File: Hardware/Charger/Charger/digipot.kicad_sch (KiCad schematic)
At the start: 8 parts, among them J1 Conn_01x03, J2 Conn_01x03, J3 Conn_01x03, J4 Conn_01x03, U1 MCP41U83x-xxxx-ST, U2 MCP41U83x-xxxx-ST, U3 MCP41U83x-xxxx-ST, U306 MCP41U83x-xxxx-ST

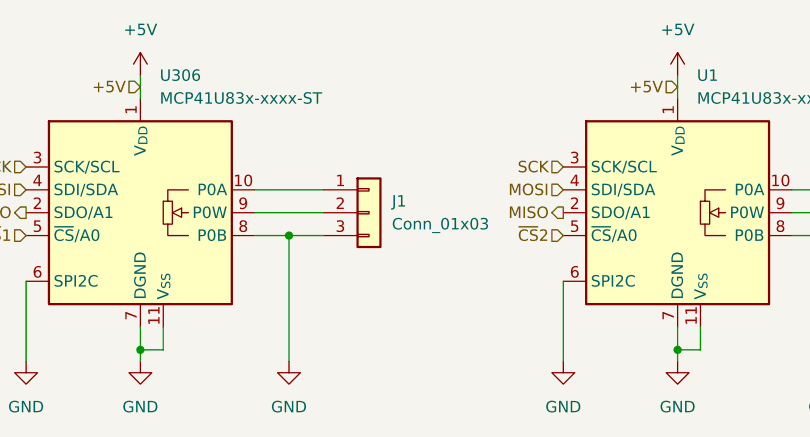
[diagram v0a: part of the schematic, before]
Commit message: Few updates to connectors
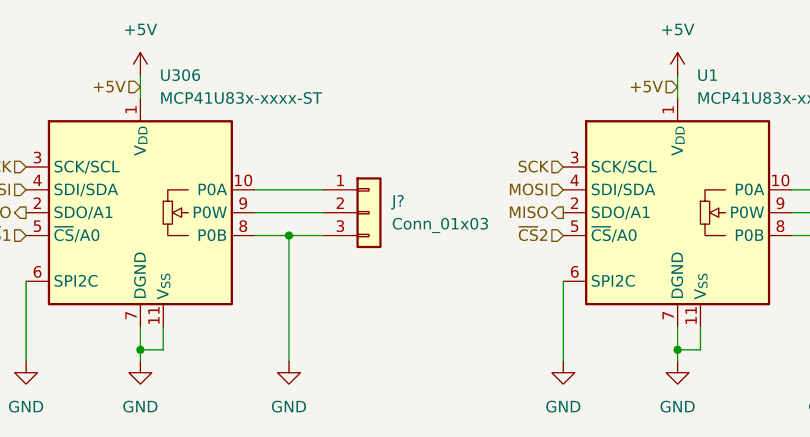
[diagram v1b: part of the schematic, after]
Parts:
- renumbered J1 to J?
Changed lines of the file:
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@@
 		(dnp no)
 		(fields_autoplaced yes)
-		(property "Reference" "#PWR01"
+		(property "Reference" "#PWR?"
 			(at 36.83 72.39 0)
 			(effects
@@
 		(pin "1"
 		)
+		(instances
+			(project "Charger"
+				(path "/ec0cb266-3da5-4155-a0e5-38a3c68d3210/b765b54b-82fb-4d18-b796-af942e7a589a"
+					(reference "#PWR?")
+					(unit 1)
+				)
+			)
+		)
 	)
 	(symbol
@@
 		(dnp no)
 		(fields_autoplaced yes)
-		(property "Reference" "J1"
+		(property "Reference" "J?"
 			(at 77.47 48.2599 0)
 			(effects
@@
 		(pin "3"
 		)
+		(instances
+			(project "Charger"
+				(path "/ec0cb266-3da5-4155-a0e5-38a3c68d3210/b765b54b-82fb-4d18-b796-af942e7a589a"
+					(reference "J?")
+					(unit 1)
+				)
+			)
+		)
 	)
 	(symbol
@@
 		(dnp no)
 		(fields_autoplaced yes)
-		(property "Reference" "#PWR04"
+		(property "Reference" "#PWR?"
 			(at 66.04 72.39 0)
 			(effects
@@
 		(pin "1"
 		)
+		(instances
+			(project "Charger"
+				(path "/ec0cb266-3da5-4155-a0e5-38a3c68d3210/b765b54b-82fb-4d18-b796-af942e7a589a"
+					(reference "#PWR?")
+					(unit 1)
+				)
+			)
+		)
 	)
 	(symbol
@@
 		(dnp no)
 		(fields_autoplaced yes)
-		(property "Reference" "#PWR03"
+		(property "Reference" "#PWR?"
 			(at 49.53 38.1 0)
 			(effects
@@
 		(pin "1"
 		)
-	)
+		(instances
+			(project "Charger"
+				(path "/ec0cb266-3da5-4155-a0e5-38a3c68d3210/b765b54b-82fb-4d18-b796-af942e7a589a"
+					(reference "#PWR?")
+					(unit 1)
+				)
+			)
+		)
+	)

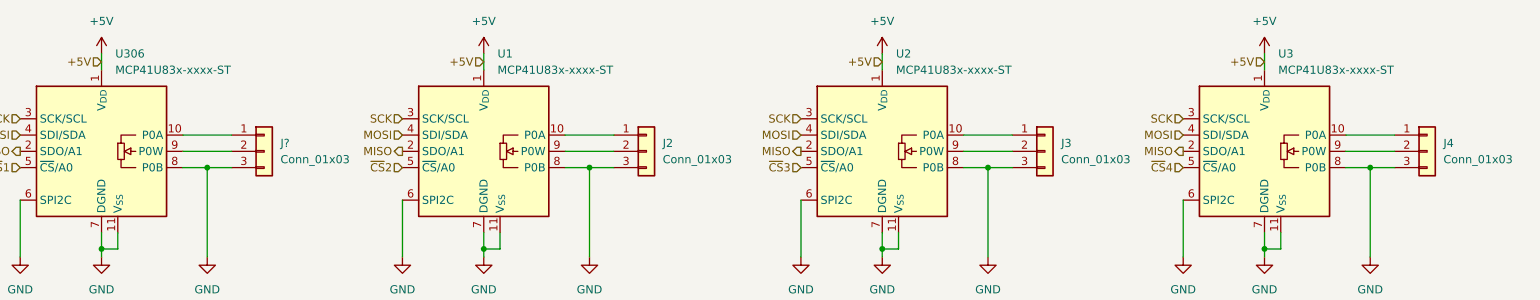
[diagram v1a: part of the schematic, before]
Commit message: Completed PCB layout of charger
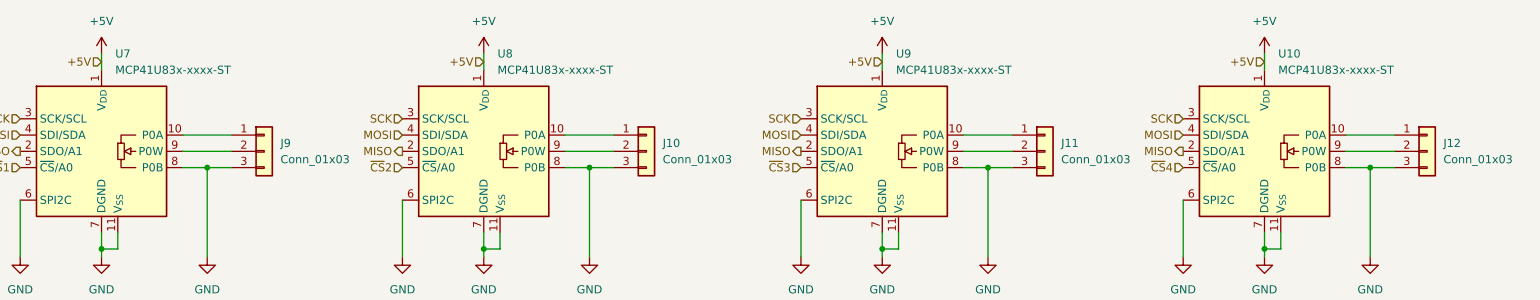
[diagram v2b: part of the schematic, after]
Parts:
- gave numbers to parts that had none: 1
- renumbered J2 to J10, J3 to J11, J4 to J12, U3 to U10, U306 to U7, U1 to U8, U2 to U9
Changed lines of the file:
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@@
 		(dnp no)
 		(fields_autoplaced yes)
-		(property "Reference" "J4"
+		(property "Reference" "J12"
 			(at 259.08 48.2599 0)
 			(effects
@@
 			(project "Charger"
 				(path "/ec0cb266-3da5-4155-a0e5-38a3c68d3210/b765b54b-82fb-4d18-b796-af942e7a589a"
-					(reference "J4")
+					(reference "J12")
 					(unit 1)
 				)
@@
 		(dnp no)
 		(fields_autoplaced yes)
-		(property "Reference" "#PWR?"
+		(property "Reference" "#PWR080"
 			(at 36.83 72.39 0)
 			(effects
@@
 			(project "Charger"
 				(path "/ec0cb266-3da5-4155-a0e5-38a3c68d3210/b765b54b-82fb-4d18-b796-af942e7a589a"
-					(reference "#PWR?")
+					(reference "#PWR080")
 					(unit 1)
 				)
@@
 		(dnp no)
 		(fields_autoplaced yes)
-		(property "Reference" "#PWR08"
+		(property "Reference" "#PWR086"
 			(at 109.22 72.39 0)
 			(effects
@@
 			(project "Charger"
 				(path "/ec0cb266-3da5-4155-a0e5-38a3c68d3210/b765b54b-82fb-4d18-b796-af942e7a589a"
-					(reference "#PWR08")
+					(reference "#PWR086")
 					(unit 1)
 				)
@@
 		(dnp no)
 		(fields_autoplaced yes)
-		(property "Reference" "#PWR09"
+		(property "Reference" "#PWR087"
 			(at 125.73 72.39 0)
 			(effects
@@
 			(project "Charger"
 				(path "/ec0cb266-3da5-4155-a0e5-38a3c68d3210/b765b54b-82fb-4d18-b796-af942e7a589a"
-					(reference "#PWR09")
+					(reference "#PWR087")
 					(unit 1)
 				)
@@
 		(dnp no)
 		(fields_autoplaced yes)
-		(property "Reference" "#PWR07"
+		(property "Reference" "#PWR085"
 			(at 109.22 38.1 0)
 			(effects
@@
 			(project "Charger"
 				(path "/ec0cb266-3da5-4155-a0e5-38a3c68d3210/b765b54b-82fb-4d18-b796-af942e7a589a"
-					(reference "#PWR07")
+					(reference "#PWR085")
 					(unit 1)
 				)
@@
 		(dnp no)
 		(fields_autoplaced yes)
-		(property "Reference" "U2"
+		(property "Reference" "U9"
 			(at 173.5933 34.29 0)
 			(effects
@@
 			(project "Charger"
 				(path "/ec0cb266-3da5-4155-a0e5-38a3c68d3210/b765b54b-82fb-4d18-b796-af942e7a589a"
-					(reference "U2")
+					(reference "U9")
 					(unit 1)
 				)
@@
 		(dnp no)
 		(fields_autoplaced yes)
-		(property "Reference" "J?"
+		(property "Reference" "J9"
 			(at 77.47 48.2599 0)
 			(effects
@@
 			(project "Charger"
 				(path "/ec0cb266-3da5-4155-a0e5-38a3c68d3210/b765b54b-82fb-4d18-b796-af942e7a589a"
-					(reference "J?")
+					(reference "J9")
 					(unit 1)
 				)
@@
 		(dnp no)
 		(fields_autoplaced yes)
-		(property "Reference" "#PWR013"
+		(property "Reference" "#PWR091"
 			(at 187.96 72.39 0)
 			(effects
@@
 			(project "Charger"
 				(path "/ec0cb266-3da5-4155-a0e5-38a3c68d3210/b765b54b-82fb-4d18-b796-af942e7a589a"
-					(reference "#PWR013")
+					(reference "#PWR091")
 					(unit 1)
 				)
@@
 		(dnp no)
 		(fields_autoplaced yes)
-		(property "Reference" "#PWR011"
+		(property "Reference" "#PWR089"
 			(at 171.45 38.1 0)
 			(effects
@@
 			(project "Charger"
 				(path "/ec0cb266-3da5-4155-a0e5-38a3c68d3210/b765b54b-82fb-4d18-b796-af942e7a589a"
-					(reference "#PWR011")
+					(reference "#PWR089")
 					(unit 1)
 				)
@@
 		(dnp no)
 		(fields_autoplaced yes)
-		(property "Reference" "#PWR02"
+		(property "Reference" "#PWR082"
 			(at 49.53 72.39 0)
 			(effects
@@
 			(project "Charger"
 				(path "/ec0cb266-3da5-4155-a0e5-38a3c68d3210/b765b54b-82fb-4d18-b796-af942e7a589a"
-					(reference "#PWR02")
+					(reference "#PWR082")
 					(unit 1)
 				)
@@
 		(dnp no)
 		(fields_autoplaced yes)
-		(property "Reference" "J2"
+		(property "Reference" "J10"
 			(at 137.16 48.2599 0)
 			(effects
@@
 			(project "Charger"
 				(path "/ec0cb266-3da5-4155-a0e5-38a3c68d3210/b765b54b-82fb-4d18-b796-af942e7a589a"
-					(reference "J2")
+					(reference "J10")
 					(unit 1)
 				)
@@
 		(dnp no)
 		(fields_autoplaced yes)
-		(property "Reference" "U1"
+		(property "Reference" "U8"
 			(at 111.3633 34.29 0)
 			(effects
@@
 			(project "Charger"
 				(path "/ec0cb266-3da5-4155-a0e5-38a3c68d3210/b765b54b-82fb-4d18-b796-af942e7a589a"
-					(reference "U1")
+					(reference "U8")
 					(unit 1)
 				)
@@
 		(dnp no)
 		(fields_autoplaced yes)
-		(property "Reference" "#PWR015"
+		(property "Reference" "#PWR093"
 			(at 231.14 38.1 0)
 			(effects
@@
 			(project "Charger"
 				(path "/ec0cb266-3da5-4155-a0e5-38a3c68d3210/b765b54b-82fb-4d18-b796-af942e7a589a"
-					(reference "#PWR015")
+					(reference "#PWR093")
 					(unit 1)
 				)
@@
 		(dnp no)
 		(fields_autoplaced yes)
-		(property "Reference" "#PWR010"
+		(property "Reference" "#PWR088"
 			(at 158.75 72.39 0)
 			(effects
@@
 			(project "Charger"
 				(path "/ec0cb266-3da5-4155-a0e5-38a3c68d3210/b765b54b-82fb-4d18-b796-af942e7a589a"
-					(reference "#PWR010")
+					(reference "#PWR088")
 					(unit 1)
 				)
@@
 		(dnp no)
 		(fields_autoplaced yes)
-		(property "Reference" "U3"
+		(property "Reference" "U10"
 			(at 233.2833 34.29 0)
 			(effects
@@
 			(project "Charger"
 				(path "/ec0cb266-3da5-4155-a0e5-38a3c68d3210/b765b54b-82fb-4d18-b796-af942e7a589a"
-					(reference "U3")
+					(reference "U10")
 					(unit 1)
 				)
@@
 		(dnp no)
 		(fields_autoplaced yes)
-		(property "Reference" "#PWR012"
+		(property "Reference" "#PWR090"
 			(at 171.45 72.39 0)
 			(effects
@@
 			(project "Charger"
 				(path "/ec0cb266-3da5-4155-a0e5-38a3c68d3210/b765b54b-82fb-4d18-b796-af942e7a589a"
-					(reference "#PWR012")
+					(reference "#PWR090")
 					(unit 1)
 				)
@@
 		(dnp no)
 		(fields_autoplaced yes)
-		(property "Reference" "#PWR017"
+		(property "Reference" "#PWR095"
 			(at 247.65 72.39 0)
 			(effects
@@
 			(project "Charger"
 				(path "/ec0cb266-3da5-4155-a0e5-38a3c68d3210/b765b54b-82fb-4d18-b796-af942e7a589a"
-					(reference "#PWR017")
+					(reference "#PWR095")
 					(unit 1)
 				)
@@
 		(dnp no)
 		(fields_autoplaced yes)
-		(property "Reference" "#PWR?"
+		(property "Reference" "#PWR083"
 			(at 66.04 72.39 0)
 			(effects
@@
 			(project "Charger"
 				(path "/ec0cb266-3da5-4155-a0e5-38a3c68d3210/b765b54b-82fb-4d18-b796-af942e7a589a"
-					(reference "#PWR?")
+					(reference "#PWR083")
 					(unit 1)
 				)
@@
 		(dnp no)
 		(fields_autoplaced yes)
-		(property "Reference" "#PWR014"
+		(property "Reference" "#PWR092"
 			(at 218.44 72.39 0)
 			(effects
@@
 			(project "Charger"
 				(path "/ec0cb266-3da5-4155-a0e5-38a3c68d3210/b765b54b-82fb-4d18-b796-af942e7a589a"
-					(reference "#PWR014")
+					(reference "#PWR092")
 					(unit 1)
 				)
@@
 		(dnp no)
 		(fields_autoplaced yes)
-		(property "Reference" "#PWR?"
+		(property "Reference" "#PWR081"
 			(at 49.53 38.1 0)
 			(effects
@@
 			(project "Charger"
 				(path "/ec0cb266-3da5-4155-a0e5-38a3c68d3210/b765b54b-82fb-4d18-b796-af942e7a589a"
-					(reference "#PWR?")
+					(reference "#PWR081")
 					(unit 1)
 				)
@@
 		(dnp no)
 		(fields_autoplaced yes)
-		(property "Reference" "U306"
+		(property "Reference" "U7"
 			(at 51.6733 34.29 0)
 			(effects
@@
 			(project "Charger"
 				(path "/ec0cb266-3da5-4155-a0e5-38a3c68d3210/b765b54b-82fb-4d18-b796-af942e7a589a"
-					(reference "U306")
+					(reference "U7")
 					(unit 1)
 				)
@@
 		(dnp no)
 		(fields_autoplaced yes)
-		(property "Reference" "#PWR016"
+		(property "Reference" "#PWR094"
 			(at 231.14 72.39 0)
 			(effects
@@
 			(project "Charger"
 				(path "/ec0cb266-3da5-4155-a0e5-38a3c68d3210/b765b54b-82fb-4d18-b796-af942e7a589a"
-					(reference "#PWR016")
+					(reference "#PWR094")
 					(unit 1)
 				)
@@
 		(dnp no)
 		(fields_autoplaced yes)
-		(property "Reference" "#PWR06"
+		(property "Reference" "#PWR084"
 			(at 96.52 72.39 0)
 			(effects
@@
 			(project "Charger"
 				(path "/ec0cb266-3da5-4155-a0e5-38a3c68d3210/b765b54b-82fb-4d18-b796-af942e7a589a"
-					(reference "#PWR06")
+					(reference "#PWR084")
 					(unit 1)
 				)
@@
 		(dnp no)
 		(fields_autoplaced yes)
-		(property "Reference" "J3"
+		(property "Reference" "J11"
 			(at 199.39 48.2599 0)
 			(effects
@@
 			(project "Charger"
 				(path "/ec0cb266-3da5-4155-a0e5-38a3c68d3210/b765b54b-82fb-4d18-b796-af942e7a589a"
-					(reference "J3")
-					(unit 1)
-				)
+					(reference "J11")
+					(unit 1)
+				)

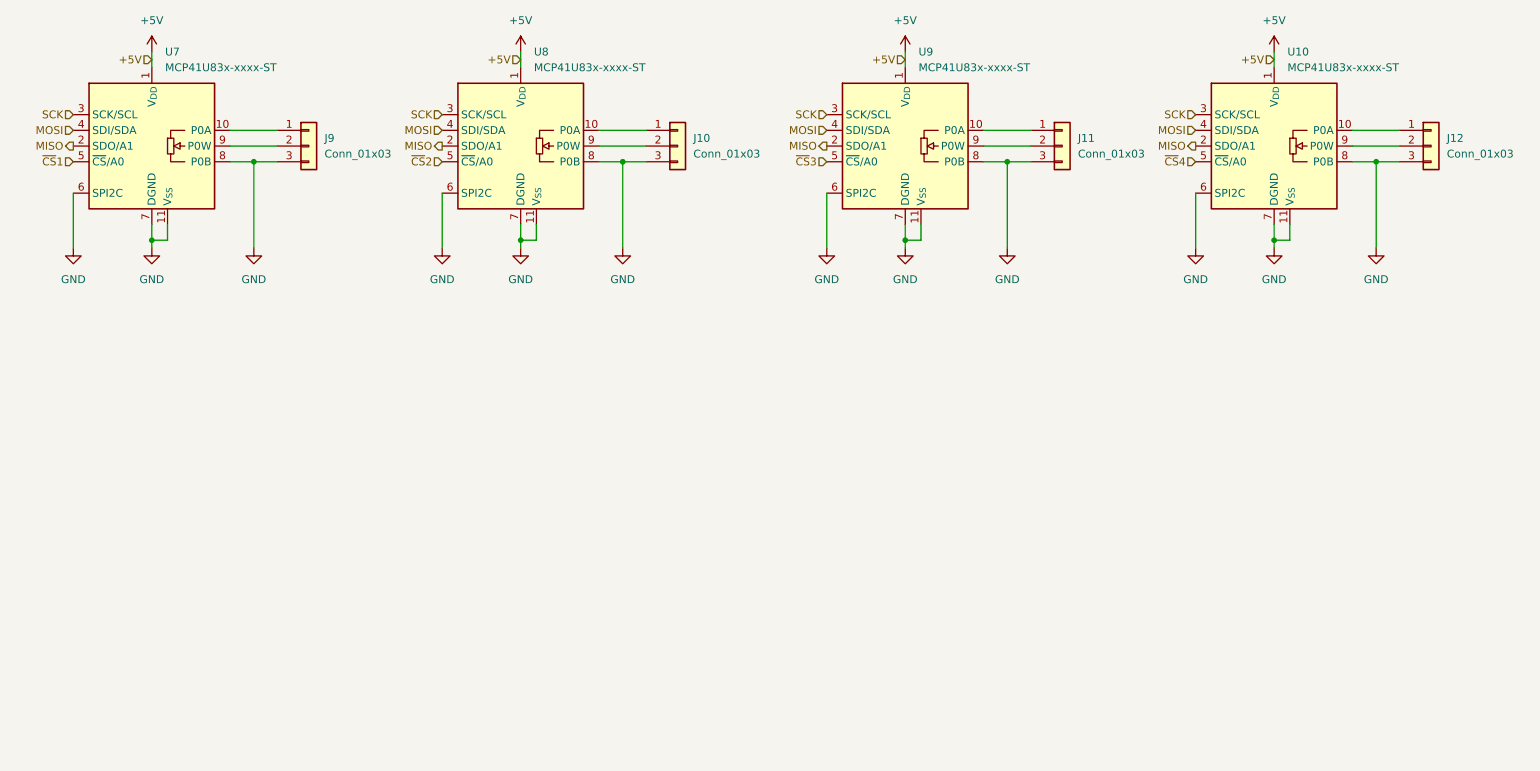
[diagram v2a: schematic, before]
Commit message: edits to charger and made ground ring bodge board. Both ready for PCB fab
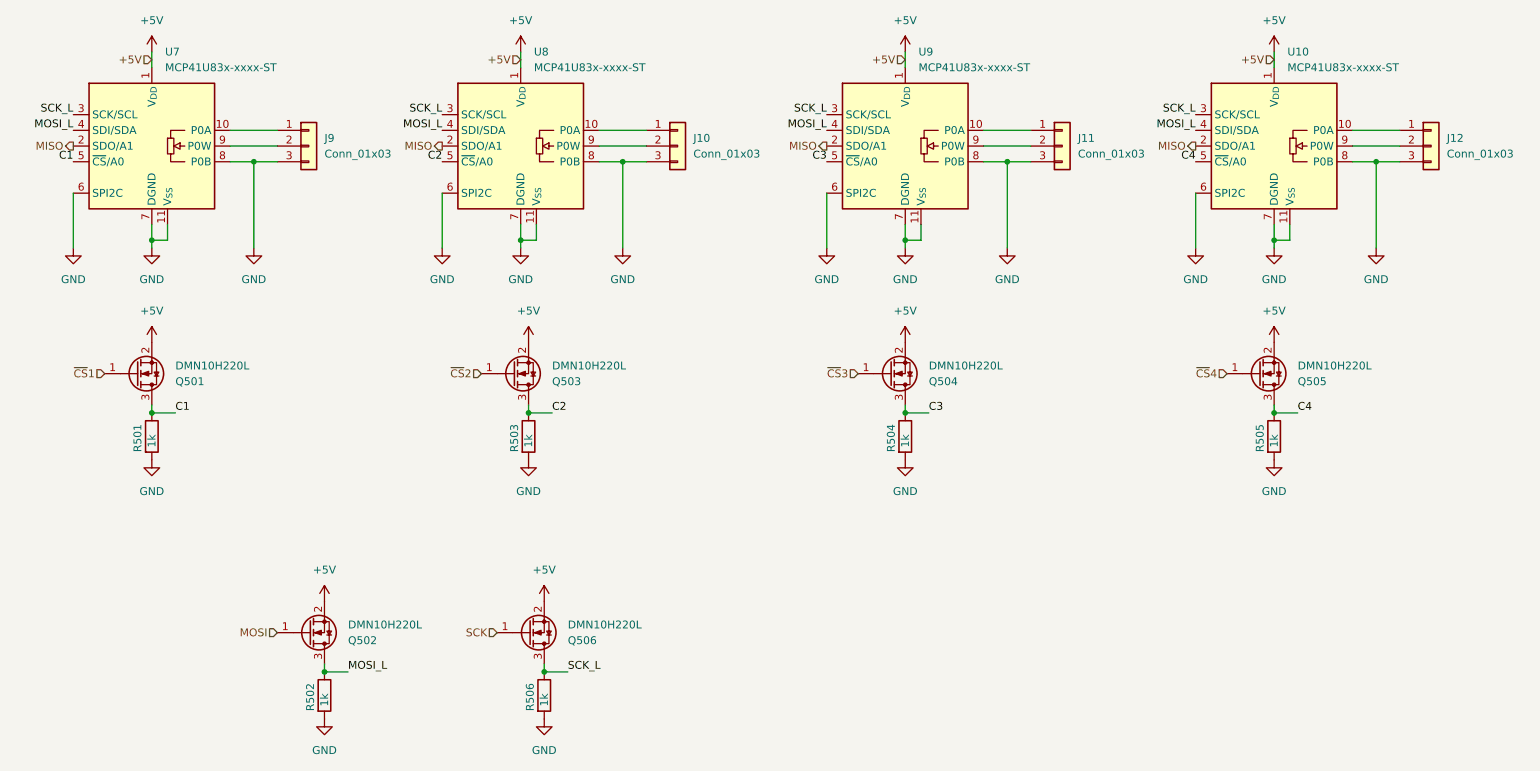
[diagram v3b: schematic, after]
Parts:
- added Q501, Q502, Q503, Q504, Q505, Q506: DMN10H220L, Package_TO_SOT_SMD:SOT-23, symbol Transistor_FET:DMN10H220L
- added R501, R502, R503, R504, R505, R506: 1k, Resistor_SMD:R_0603_1608Metric, symbol OEM:120R_DNP
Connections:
- net +5V: now also Q501.2 (S), Q502.2 (S), Q503.2 (S), Q504.2 (S), Q505.2 (S), Q506.2 (S)
- net GND: now also R501.2, R502.2, R503.2, R504.2, R505.2, R506.2
- net MOSI: now also Q502.1 (G); no longer U10.4 (SDI/SDA), U7.4 (SDI/SDA), U8.4 (SDI/SDA), U9.4 (SDI/SDA)
- net SCK: now also Q506.1 (G); no longer U10.3 (SCK/SCL), U7.3 (SCK/SCL), U8.3 (SCK/SCL), U9.3 (SCK/SCL)
- net ~{CS}1: now also Q501.1 (G); no longer U7.5 (~{CS}/A0)
- net ~{CS}2: now also Q503.1 (G); no longer U8.5 (~{CS}/A0)
- net ~{CS}3: now also Q504.1 (G); no longer U9.5 (~{CS}/A0)
- net ~{CS}4: now also Q505.1 (G); no longer U10.5 (~{CS}/A0)
- new net C1: Q501.3 (D), R501.1, U7.5 (~{CS}/A0)
- new net C2: Q503.3 (D), R503.1, U8.5 (~{CS}/A0)
- new net C3: Q504.3 (D), R504.1, U9.5 (~{CS}/A0)
- new net C4: Q505.3 (D), R505.1, U10.5 (~{CS}/A0)
- new net MOSI_L: Q502.3 (D), R502.1, U10.4 (SDI/SDA), U7.4 (SDI/SDA), U8.4 (SDI/SDA), U9.4 (SDI/SDA)
- new net SCK_L: Q506.3 (D), R506.1, U10.3 (SCK/SCL), U7.3 (SCK/SCL), U8.3 (SCK/SCL), U9.3 (SCK/SCL)
